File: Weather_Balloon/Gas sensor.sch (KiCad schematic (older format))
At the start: 6 parts

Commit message: Logging packed
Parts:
- added R?: 4.22k, symbol R
- added R? (x3): 27R, symbol R
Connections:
- net +5V: now also R?.1
- net GND: now also R?.2, R?.2
- net at U?.5 (Ref): now also R?.1, R?.1, R?.1
- new net: R?.2, R?.2
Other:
- moved on the sheet: C?
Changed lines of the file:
@@
 $Descr A4 11693 8268
 encoding utf-8
-Sheet 3 3
+Sheet 3 4
 Title ""
 Date ""
@@
 	4900 1950 4950 1950
 Wire Wire Line
-	4950 1950 4950 2600
+	4950 1950 4950 2050
+Wire Wire Line
+	4950 2050 4950 2150
+Wire Wire Line
+	4950 2150 4950 2250
+Wire Wire Line
+	4950 2250 4950 2350
+Wire Wire Line
+	4950 2350 4950 2500
+Wire Wire Line
+	4950 2500 4950 2600
 Wire Wire Line
 	3800 2050 3750 2050
 Wire Wire Line
-	3750 2050 3750 2500
-Wire Wire Line
-	3750 2500 5150 2500
+	3750 2050 3750 2150
+Wire Wire Line
+	3750 2150 3750 2250
+Wire Wire Line
+	3750 2250 3750 2350
+Wire Wire Line
+	3750 2350 3750 2500
+Wire Wire Line
+	3750 2500 4950 2500
+Wire Wire Line
+	4950 2500 5150 2500
 Connection ~ 4950 2500
 Wire Wire Line
@@
 L C C?
 U 1 1 57DCD5CF
-P 6950 1500
-F 0 "C?" H 7065 1546 50  0000 L CNN
-F 1 "0.1uF" H 7065 1455 50  0000 L CNN
-F 2 "" H 6988 1350 50  0000 C CNN
-F 3 "" H 6950 1500 50  0000 C CNN
-	1    6950 1500
+P 6950 1300
+F 0 "C?" H 7065 1346 50  0000 L CNN
+F 1 "0.1uF" H 7065 1255 50  0000 L CNN
+F 2 "" H 6988 1150 50  0000 C CNN
+F 3 "" H 6950 1300 50  0000 C CNN
+	1    6950 1300
 	1    0    0    -1
 $EndComp
@@
 L C C?
 U 1 1 57DCD5D6
-P 7400 1500
-F 0 "C?" H 7515 1546 50  0000 L CNN
-F 1 "22uF" H 7515 1455 50  0000 L CNN
-F 2 "" H 7438 1350 50  0000 C CNN
-F 3 "" H 7400 1500 50  0000 C CNN
-	1    7400 1500
+P 7400 1300
+F 0 "C?" H 7515 1346 50  0000 L CNN
+F 1 "22uF" H 7515 1255 50  0000 L CNN
+F 2 "" H 7438 1150 50  0000 C CNN
+F 3 "" H 7400 1300 50  0000 C CNN
+	1    7400 1300
 	1    0    0    -1
 $EndComp
@@
 L +5V #PWR?
 U 1 1 57DCD5DD
-P 7750 1250
-F 0 "#PWR?" H 7750 1100 50  0001 C CNN
-F 1 "+5V" H 7765 1423 50  0000 C CNN
-F 2 "" H 7750 1250 50  0000 C CNN
-F 3 "" H 7750 1250 50  0000 C CNN
-	1    7750 1250
-	1    0    0    -1
-$EndComp
-Wire Wire Line
-	7750 1250 7750 1900
-Wire Wire Line
-	6950 1350 6950 1300
-Wire Wire Line
-	6950 1300 7750 1300
-Connection ~ 7750 1300
-Wire Wire Line
-	7400 1350 7400 1300
-Connection ~ 7400 1300
+P 7750 850
+F 0 "#PWR?" H 7750 700 50  0001 C CNN
+F 1 "+5V" H 7765 1023 50  0000 C CNN
+F 2 "" H 7750 850 50  0000 C CNN
+F 3 "" H 7750 850 50  0000 C CNN
+	1    7750 850
+	1    0    0    -1
+$EndComp
+Wire Wire Line
+	7750 850  7750 1100
+Wire Wire Line
+	7750 1100 7750 1900
+Wire Wire Line
+	6950 1150 6950 1100
+Wire Wire Line
+	6950 1100 7400 1100
+Wire Wire Line
+	7400 1100 7750 1100
+Wire Wire Line
+	7750 1100 7900 1100
+Connection ~ 7750 1100
+Wire Wire Line
+	7400 1150 7400 1100
+Connection ~ 7400 1100
 $Comp
 L GND #PWR?
 U 1 1 57DCD5E9
-P 7200 1750
-F 0 "#PWR?" H 7200 1500 50  0001 C CNN
-F 1 "GND" H 7205 1577 50  0000 C CNN
-F 2 "" H 7200 1750 50  0000 C CNN
-F 3 "" H 7200 1750 50  0000 C CNN
-	1    7200 1750
-	1    0    0    -1
-$EndComp
-Wire Wire Line
-	6950 1650 6950 1700
-Wire Wire Line
-	6950 1700 7400 1700
-Wire Wire Line
-	7400 1700 7400 1650
-Wire Wire Line
-	7200 1750 7200 1700
-Connection ~ 7200 1700
+P 7200 1550
+F 0 "#PWR?" H 7200 1300 50  0001 C CNN
+F 1 "GND" H 7205 1377 50  0000 C CNN
+F 2 "" H 7200 1550 50  0000 C CNN
+F 3 "" H 7200 1550 50  0000 C CNN
+	1    7200 1550
+	1    0    0    -1
+$EndComp
+Wire Wire Line
+	6950 1450 6950 1500
+Wire Wire Line
+	6950 1500 7200 1500
+Wire Wire Line
+	7200 1500 7400 1500
+Wire Wire Line
+	7400 1500 7400 1450
+Wire Wire Line
+	7200 1550 7200 1500
+Connection ~ 7200 1500
 $Comp
 L GND #PWR?
@@
 	7550 2300 7500 2300
 Wire Wire Line
-	7500 2300 7500 2650
+	7500 2300 7500 2550
+Wire Wire Line
+	7500 2550 7500 2650
 Wire Wire Line
 	7500 2550 7750 2550
@@
 Wire Wire Line
 	8300 2200 8150 2200
+$Comp
+L R R?
+U 1 1 57E7B560
+P 8050 1100
+F 0 "R?" V 8150 1100 50  0000 L CNN
+F 1 "4.22k" V 7950 1000 50  0000 L CNN
+F 2 "" V 7980 1100 50  0000 C CNN
+F 3 "" H 8050 1100 50  0000 C CNN
+	1    8050 1100
+	0    -1   -1   0
+$EndComp
+$Comp
+L R R?
+U 1 1 57E7B66B
+P 8650 1650
+F 0 "R?" H 8720 1696 50  0000 L CNN
+F 1 "27R" V 8650 1600 50  0000 L CNN
+F 2 "" V 8580 1650 50  0000 C CNN
+F 3 "" H 8650 1650 50  0000 C CNN
+	1    8650 1650
+	1    0    0    -1
+$EndComp
+$Comp
+L R R?
+U 1 1 57E7B6E8
+P 8400 1100
+F 0 "R?" V 8300 1000 50  0000 L CNN
+F 1 "27R" V 8400 1050 50  0000 L CNN
+F 2 "" V 8330 1100 50  0000 C CNN
+F 3 "" H 8400 1100 50  0000 C CNN
+	1    8400 1100
+	0    1    1    0
+$EndComp
+$Comp
+L R R?
+U 1 1 57E7B826
+P 8900 1650
+F 0 "R?" H 8970 1696 50  0000 L CNN
+F 1 "27R" V 8900 1600 50  0000 L CNN
+F 2 "" V 8830 1650 50  0000 C CNN
+F 3 "" H 8900 1650 50  0000 C CNN
+	1    8900 1650
+	1    0    0    -1
+$EndComp
+$Comp
+L GND #PWR?
+U 1 1 57E7B888
+P 8650 1900
+F 0 "#PWR?" H 8650 1650 50  0001 C CNN
+F 1 "GND" H 8655 1727 50  0000 C CNN
+F 2 "" H 8650 1900 50  0000 C CNN
+F 3 "" H 8650 1900 50  0000 C CNN
+	1    8650 1900
+	1    0    0    -1
+$EndComp
+Wire Wire Line
+	8200 1100 8250 1100
+Wire Wire Line
+	8650 1100 8650 1450
+Wire Wire Line
+	8650 1450 8650 1500
+Wire Wire Line
+	7850 1450 8650 1450
+Wire Wire Line
+	8650 1450 8900 1450
+Wire Wire Line
+	8900 1450 8900 1500
+Wire Wire Line
+	8650 1800 8650 1850
+Wire Wire Line
+	8650 1850 8650 1900
+Wire Wire Line
+	8900 1800 8900 1850
+Wire Wire Line
+	8900 1850 8650 1850
+Connection ~ 8650 1850
+Connection ~ 8650 1450
+Wire Wire Line
+	7850 1900 7850 1450
+Wire Wire Line
+	8650 1100 8550 1100
 $EndSCHEMATC

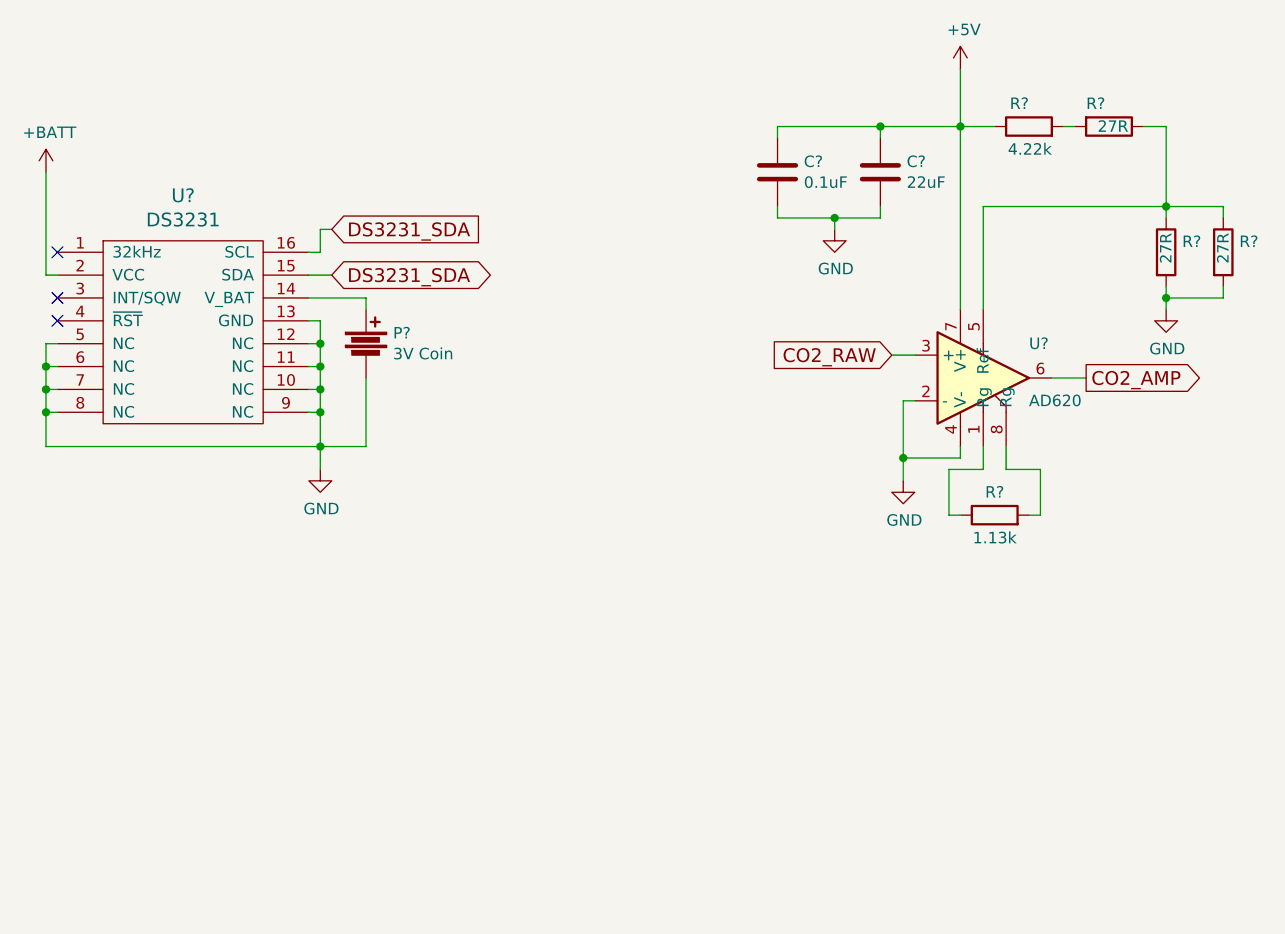
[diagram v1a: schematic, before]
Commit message: Initial PCB design with throughhole components. Layout not finilized.
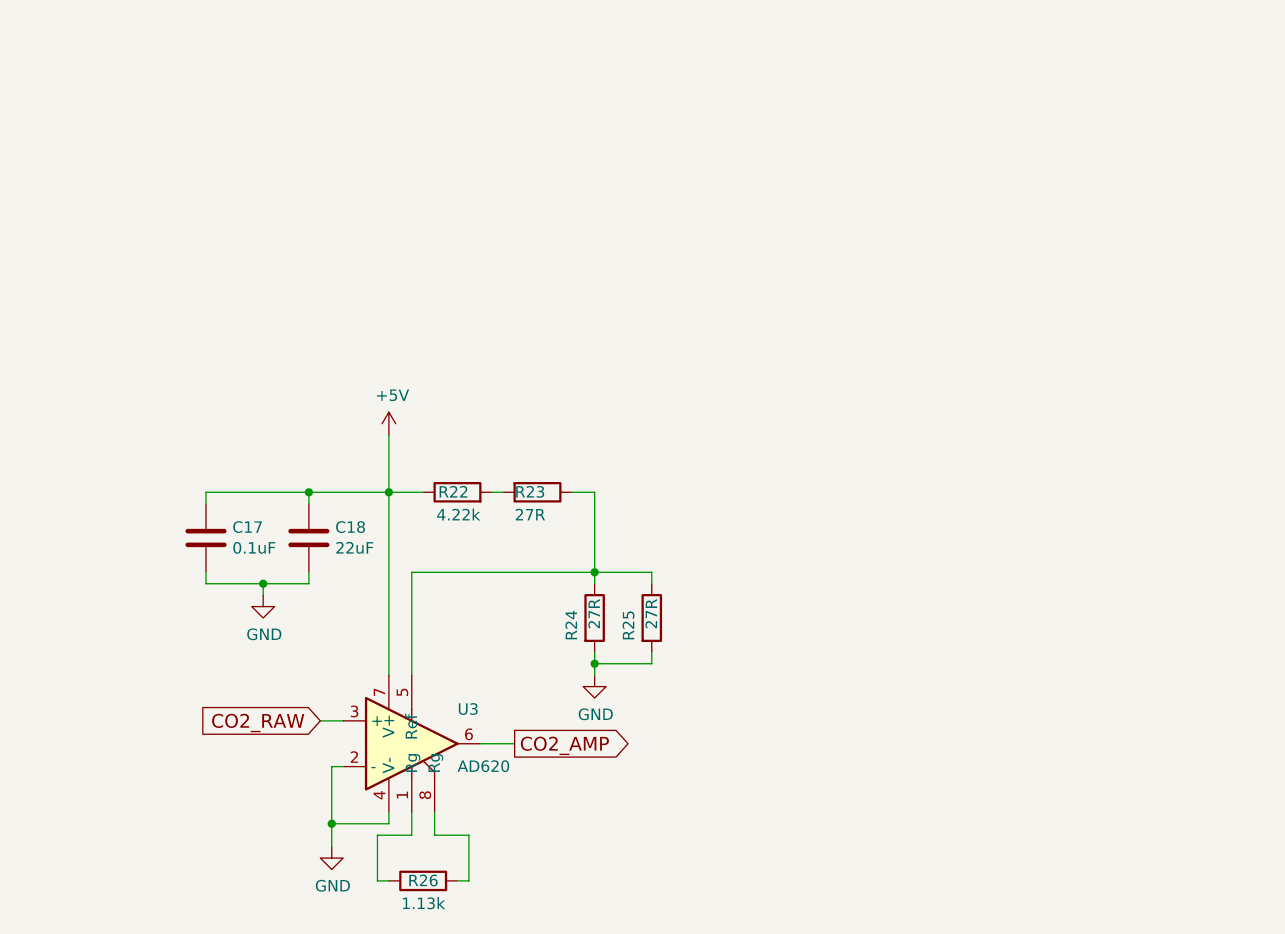
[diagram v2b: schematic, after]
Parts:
- removed P?: 3V Coin, symbol Battery
- removed U?: DS3231, symbol DS3231
- gave numbers to parts that had none: 8
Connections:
- no-connect marks 3 -> 0
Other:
- moved on the sheet: C17, C18, R22, R23, R24, R25, R26, U3
